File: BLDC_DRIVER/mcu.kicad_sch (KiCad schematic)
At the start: 0 parts

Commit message: buck and mcu added
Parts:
- added U2: STM32G431RBTx, Package_QFP:LQFP-64_10x10mm_P0.5mm, symbol MCU_ST_STM32G4:STM32G431RBTx
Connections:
- new net: U2.15 (VSS), U2.31 (VSS), U2.47 (VSS), U2.63 (VSS)
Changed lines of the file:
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@@
 	(generator_version "9.0")
 	(paper "A4")
+	(symbol
+		(lib_id "MCU_ST_STM32G4:STM32G431RBTx")
+		(at 92.71 85.09 0)
+		(unit 1)
+		(exclude_from_sim no)
+		(in_bom yes)
+		(on_board yes)
+		(dnp no)
+		(fields_autoplaced yes)
+		(property "Reference" "U2"
+			(at 97.3933 133.35 0)
+			(effects
+				(font
+					(size 1.27 1.27)
+				)
+				(justify left)
+			)
+		)
+		(property "Value" "STM32G431RBTx"
+			(at 97.3933 135.89 0)
+			(effects
+				(font
+					(size 1.27 1.27)
+				)
+				(justify left)
+			)
+		)
+		(property "Footprint" "Package_QFP:LQFP-64_10x10mm_P0.5mm"
+			(at 77.47 130.81 0)
+			(effects
+				(font
+					(size 1.27 1.27)
+				)
+				(justify right)
+				(hide yes)
+			)
+		)
+		(property "Datasheet" "https://www.st.com/resource/en/datasheet/stm32g431rb.pdf"
+			(at 92.71 85.09 0)
+			(effects
+				(font
+					(size 1.27 1.27)
+				)
+				(hide yes)
+			)
+		)
+		(property "Description" "STMicroelectronics Arm Cortex-M4 MCU, 128KB flash, 32KB RAM, 170 MHz, 1.71-3.6V, 52 GPIO, LQFP64"
+			(at 92.71 85.09 0)
+			(effects
+				(font
+					(size 1.27 1.27)
+				)
+				(hide yes)
+			)
+		)
+		(pin "16"
+		)
+		(pin "27"
+		)
+		(pin "53"
+		)
+		(pin "55"
+		)
+		(pin "9"
+		)
+		(pin "48"
+		)
+		(pin "23"
+		)
+		(pin "45"
+		)
+		(pin "4"
+		)
+		(pin "22"
+		)
+		(pin "29"
+		)
+		(pin "52"
+		)
+		(pin "21"
+		)
+		(pin "57"
+		)
+		(pin "15"
+		)
+		(pin "7"
+		)
+		(pin "3"
+		)
+		(pin "58"
+		)
+		(pin "11"
+		)
+		(pin "10"
+		)
+		(pin "64"
+		)
+		(pin "24"
+		)
+		(pin "12"
+		)
+		(pin "39"
+		)
+		(pin "47"
+		)
+		(pin "2"
+		)
+		(pin "17"
+		)
+		(pin "28"
+		)
+		(pin "41"
+		)
+		(pin "31"
+		)
+		(pin "19"
+		)
+		(pin "20"
+		)
+		(pin "40"
+		)
+		(pin "38"
+		)
+		(pin "6"
+		)
+		(pin "1"
+		)
+		(pin "32"
+		)
+		(pin "5"
+		)
+		(pin "8"
+		)
+		(pin "54"
+		)
+		(pin "63"
+		)
+		(pin "14"
+		)
+		(pin "13"
+		)
+		(pin "18"
+		)
+		(pin "42"
+		)
+		(pin "43"
+		)
+		(pin "44"
+		)
+		(pin "46"
+		)
+		(pin "49"
+		)
+		(pin "50"
+		)
+		(pin "51"
+		)
+		(pin "26"
+		)
+		(pin "25"
+		)
+		(pin "56"
+		)
+		(pin "61"
+		)
+		(pin "59"
+		)
+		(pin "62"
+		)
+		(pin "30"
+		)
+		(pin "35"
+		)
+		(pin "37"
+		)
+		(pin "36"
+		)
+		(pin "60"
+		)
+		(pin "33"
+		)
+		(pin "34"
+		)
+		(instances
+			(project ""
+				(path "/3fb7c58e-7fa7-4c2f-8afc-969dd7f24a74/3858e4a6-498a-4dbf-a28d-a3d68cd1c461"
+					(reference "U2")
+					(unit 1)
+				)
+			)
+		)
+	)
 )

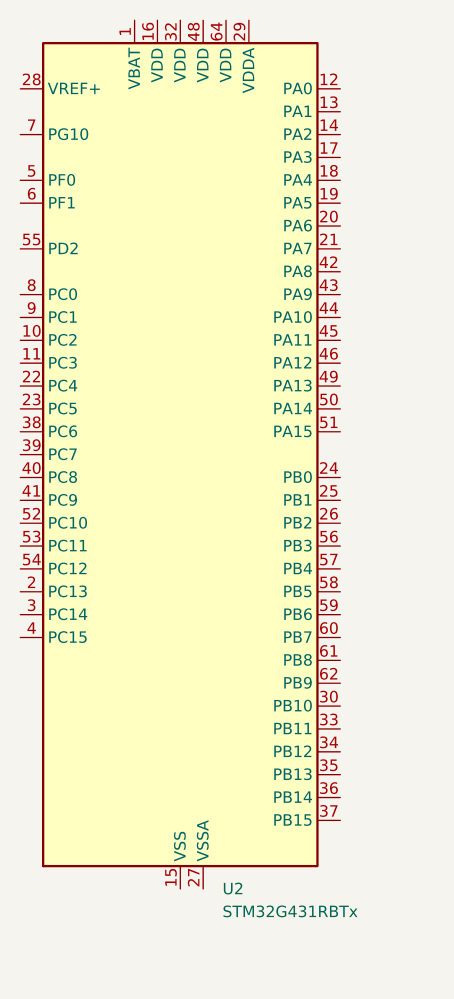
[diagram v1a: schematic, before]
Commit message: ldo added
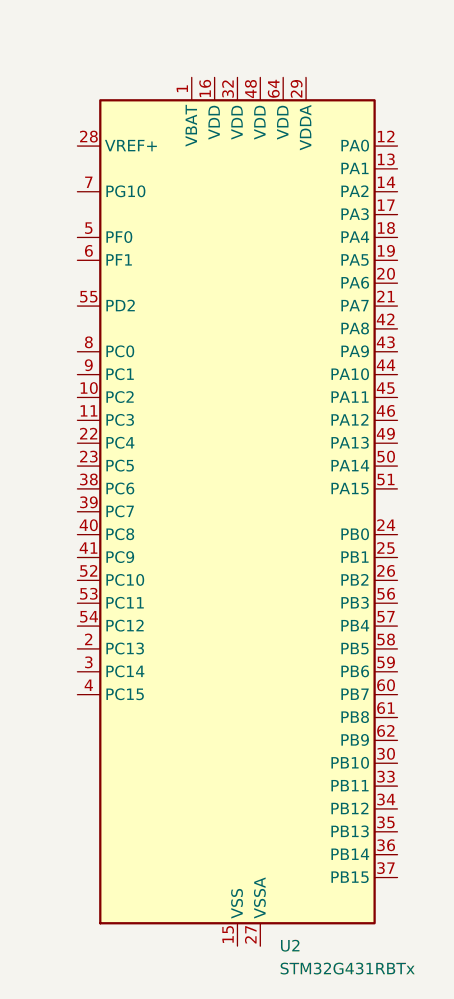
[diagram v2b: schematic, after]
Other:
- moved on the sheet: U2
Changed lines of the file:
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@@
 	(symbol
 		(lib_id "MCU_ST_STM32G4:STM32G431RBTx")
-		(at 92.71 85.09 0)
+		(at 99.06 91.44 0)
 		(unit 1)
 		(exclude_from_sim no)
@@
 		(fields_autoplaced yes)
 		(property "Reference" "U2"
-			(at 97.3933 133.35 0)
+			(at 103.7433 139.7 0)
 			(effects
 				(font
@@
 		)
 		(property "Value" "STM32G431RBTx"
-			(at 97.3933 135.89 0)
+			(at 103.7433 142.24 0)
 			(effects
 				(font
@@
 		)
 		(property "Footprint" "Package_QFP:LQFP-64_10x10mm_P0.5mm"
-			(at 77.47 130.81 0)
+			(at 83.82 137.16 0)
 			(effects
 				(font
@@
 		)
 		(property "Datasheet" "https://www.st.com/resource/en/datasheet/stm32g431rb.pdf"
-			(at 92.71 85.09 0)
+			(at 99.06 91.44 0)
 			(effects
 				(font
@@
 		)
 		(property "Description" "STMicroelectronics Arm Cortex-M4 MCU, 128KB flash, 32KB RAM, 170 MHz, 1.71-3.6V, 52 GPIO, LQFP64"
-			(at 92.71 85.09 0)
+			(at 99.06 91.44 0)
 			(effects
 				(font

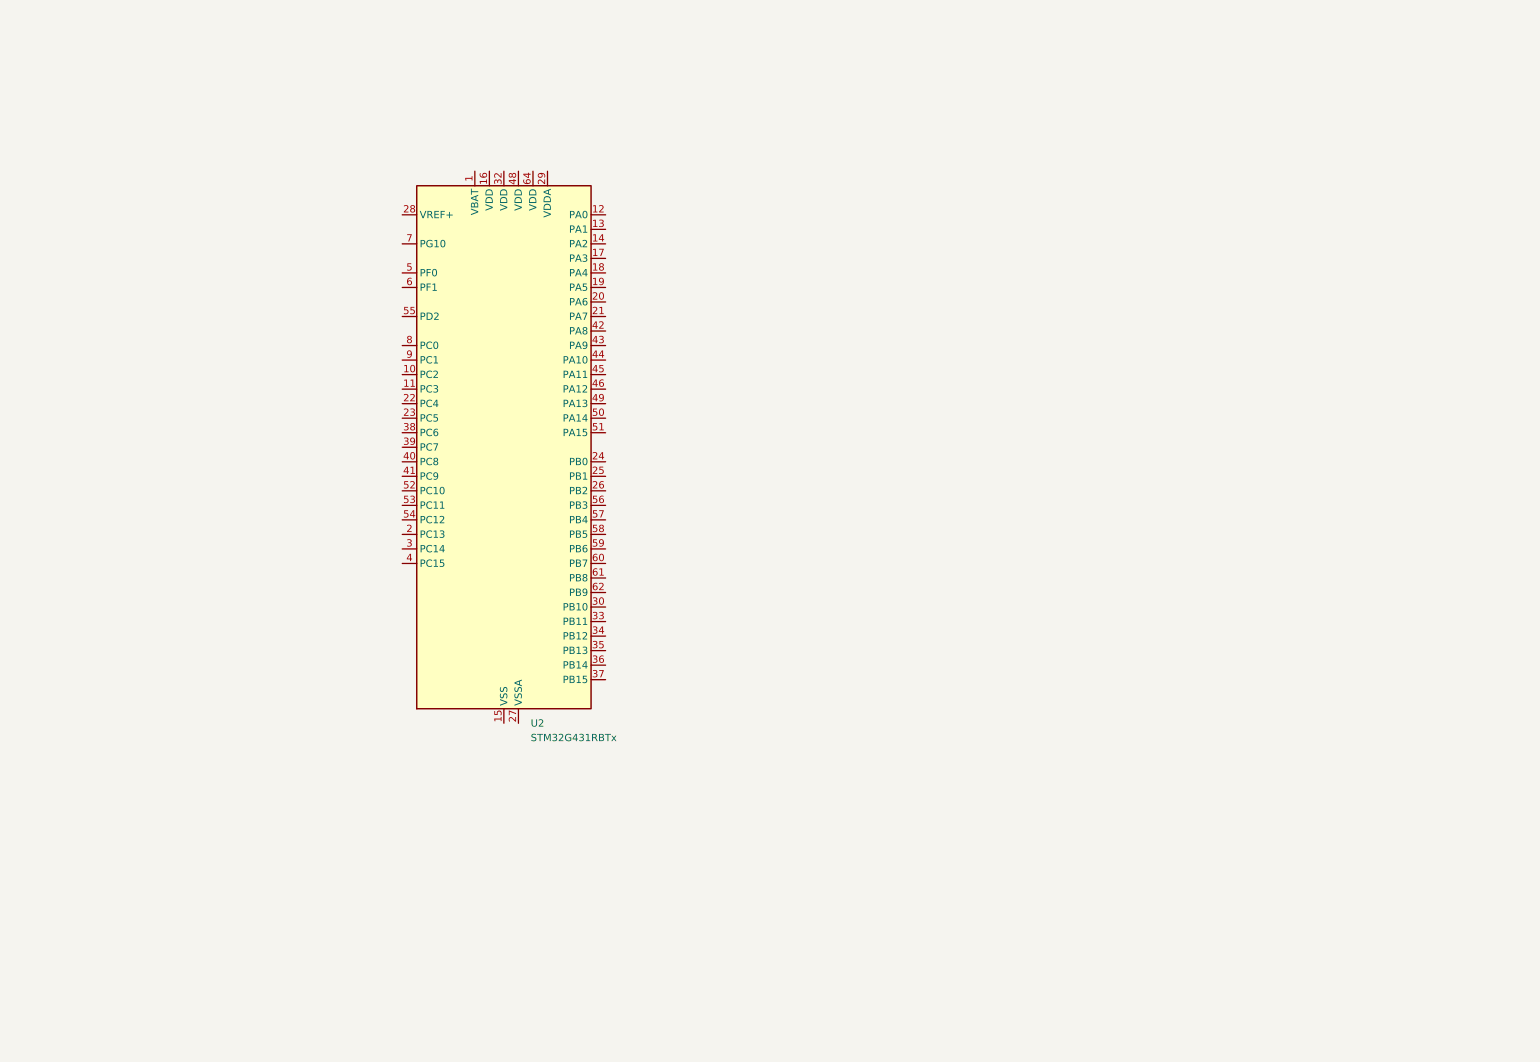
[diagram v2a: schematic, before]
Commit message: mcu added
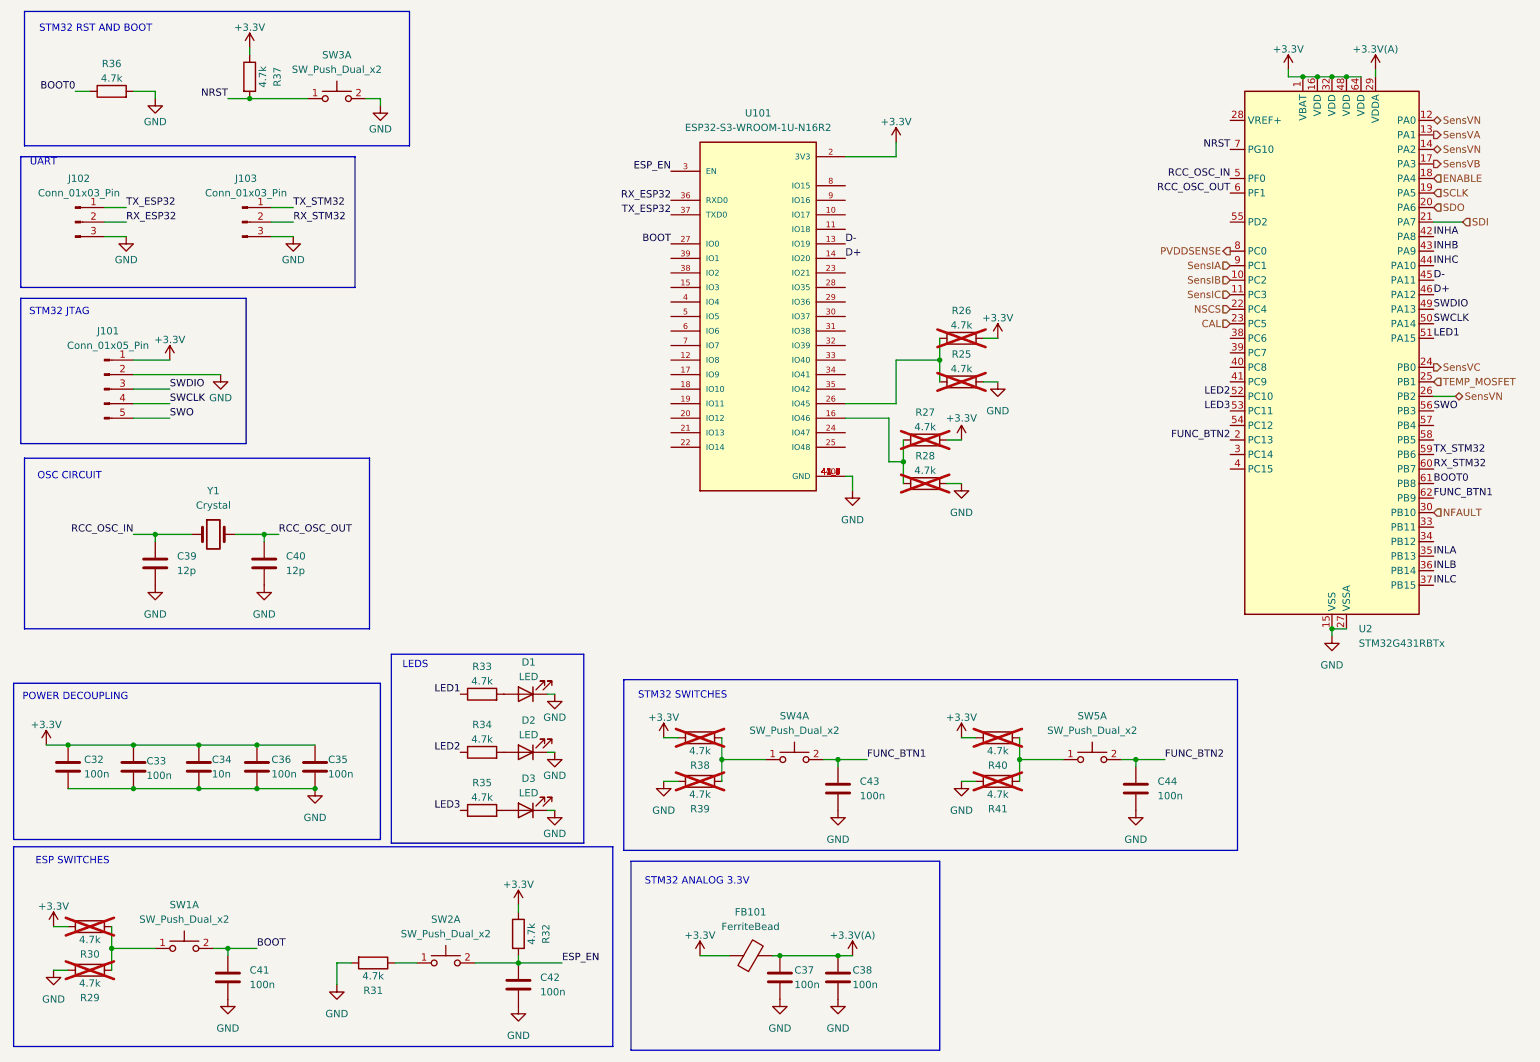
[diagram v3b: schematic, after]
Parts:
- added C32, C33, C35, C36, C37, C38, C41, C42, C43, C44: 100n, symbol Device:C
- added C34: 10n, symbol Device:C
- added C39, C40: 12p, symbol Device:C
- added D1, D2, D3: LED, symbol Device:LED
- added FB101: FerriteBead, symbol Device:FerriteBead
- added J101: Conn_01x05_Pin, symbol Connector:Conn_01x05_Pin
- added J102, J103: Conn_01x03_Pin, symbol Connector:Conn_01x03_Pin
- added R25, R26, R27, R28, R29, R30, R31, R32, R33, R34, R35, R36, R37, R38, R39, R40, R41: 4.7k, symbol Device:R
- added SW1, SW2, SW3, SW4, SW5: SW_Push_Dual_x2, Button_Switch_SMD:SW_Push_1P1T_NO_CK_KSC7xxJ, symbol Switch:SW_Push_Dual_x2
- added U101: ESP32-S3-WROOM-1U-N16R2, ESP32-S3-WROOM-1U-N16R2:XCVR_ESP32-S3-WROOM-1U-N16R2, symbol ESP32-S3-WROOM-1U-N16R2:ESP32-S3-WROOM-1U-N16R2
- added Y1: Crystal, symbol Device:Crystal
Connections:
- net +3.3V: now reaches U2.1 (VBAT)
- net +3.3V: now also U2.16 (VDD), U2.32 (VDD), U2.48 (VDD), U2.64 (VDD), C32.2, C33.2, C34.2, C35.2, C36.2, FB101.1, J101.1 (Pin_1), R26.2, R27.2, R30.2, R32.1, R37.1, R38.2, R40.2, U101.2 (3V3)
- net SensIB: now reaches U2.10 (PC2)
- net SensIC: now reaches U2.11 (PC3)
- net SensVN: now reaches U2.12 (PA0)
- net SensVN: now also U2.14 (PA2), U2.26 (PB2)
- net SensVA: now reaches U2.13 (PA1)
- net GND: now reaches U2.15 (VSS), U2.31 (VSS), U2.47 (VSS), U2.63 (VSS)
- net GND: now also U2.27 (VSSA), C32.1, C33.1, C34.1, C35.1, C36.1, C37.1, C38.1, C39.1, C40.1, C41.1, C42.1, C43.1, C44.1, D1.1 (K), D2.1 (K), D3.1 (K), J101.2 (Pin_2), J102.3 (Pin_3), J103.3 (Pin_3), R25.2, R28.2, R29.2, R31.2, R36.2, R39.2, R41.2, SW3.2 (D), U101.1 (GND), U101.40 (GND), U101.41_1 (GND), U101.41_2 (GND), U101.41_3 (GND), U101.41_4 (GND), U101.41_5 (GND), U101.41_6 (GND), U101.41_7 (GND), U101.41_8 (GND), U101.41_9 (GND)
- net SensVB: now reaches U2.17 (PA3)
- net ENABLE: now reaches U2.18 (PA4)
- net SCLK: now reaches U2.19 (PA5)
- net FUNC_BTN2: now reaches U2.2 (PC13)
- net FUNC_BTN2: now also C44.2, SW5.2 (D)
- net SDO: now reaches U2.20 (PA6)
- net SDI: now reaches U2.21 (PA7)
- net NSCS: now reaches U2.22 (PC4)
- net CAL: now reaches U2.23 (PC5)
- net SensVC: now reaches U2.24 (PB0)
- net TEMP_MOSFET: now reaches U2.25 (PB1)
- net +3.3V(A): now reaches U2.29 (VDDA)
- net +3.3V(A): now also C37.2, C38.2, FB101.2
- net NFAULT: now reaches U2.30 (PB10)
- net INLA: now reaches U2.35 (PB13)
- net INLB: now reaches U2.36 (PB14)
- net INLC: now reaches U2.37 (PB15)
- net INHA: now reaches U2.42 (PA8)
- net INHB: now reaches U2.43 (PA9)
- net INHC: now reaches U2.44 (PA10)
- net D-: now reaches U2.45 (PA11)
- net D-: now also U101.13 (IO19)
- net D+: now reaches U2.46 (PA12)
- net D+: now also U101.14 (IO20)
- net SWDIO: now reaches U2.49 (PA13)
- net SWDIO: now also J101.3 (Pin_3)
- net RCC_OSC_IN: now reaches U2.5 (PF0)
- net RCC_OSC_IN: now also C39.2, Y1.1
- net SWCLK: now reaches U2.50 (PA14)
- net SWCLK: now also J101.4 (Pin_4)
- net LED1: now reaches U2.51 (PA15)
- net LED1: now also R33.1
- net LED2: now reaches U2.52 (PC10)
- net LED2: now also R34.1
- net LED3: now reaches U2.53 (PC11)
- net LED3: now also R35.1
- net SWO: now reaches U2.56 (PB3)
- net SWO: now also J101.5 (Pin_5)
- net TX_STM32: now reaches U2.59 (PB6)
- net TX_STM32: now also J103.1 (Pin_1)
- net RCC_OSC_OUT: now reaches U2.6 (PF1)
- net RCC_OSC_OUT: now also C40.2, Y1.2
- net RX_STM32: now reaches U2.60 (PB7)
- net RX_STM32: now also J103.2 (Pin_2)
- net BOOT0: now reaches U2.61 (PB8)
- net BOOT0: now also R36.1
- net FUNC_BTN1: now reaches U2.62 (PB9)
- net FUNC_BTN1: now also C43.2, SW4.2 (D)
- net NRST: now reaches U2.7 (PG10)
- net NRST: now also R37.2, SW3.1 (C)
- net PVDDSENSE: now reaches U2.8 (PC0)
- net SensIA: now reaches U2.9 (PC1)
- new net: R29.1, R30.1, SW1.1 (C)
- new net: D2.2 (A), R34.2
- new net: D1.2 (A), R33.2
- new net: R25.1, R26.1, U101.26 (IO45)
- new net: R38.1, R39.1, SW4.1 (C)
- new net: D3.2 (A), R35.2
- new net: R27.1, R28.1, U101.16 (IO46)
- new net: R40.1, R41.1, SW5.1 (C)
- new net: R31.1, SW2.1 (C)
- new net BOOT: C41.2, SW1.2 (D), U101.27 (IO0)
- new net ESP_EN: C42.2, R32.2, SW2.2 (D), U101.3 (EN)
- new net RX_ESP32: J102.2 (Pin_2), U101.36 (RXD0)
- new net TX_ESP32: J102.1 (Pin_1), U101.37 (TXD0)
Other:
- note added: "ESP SWITCHES"
- note added: "LEDS"
- note added: "OSC CIRCUIT"
- note added: "POWER DECOUPLING"
- note added: "STM32 ANALOG 3.3V"
- note added: "STM32 JTAG"
- note added: "STM32 RST AND BOOT"
- note added: "STM32 SWITCHES"
- note added: "UART"
- moved on the sheet: U2
